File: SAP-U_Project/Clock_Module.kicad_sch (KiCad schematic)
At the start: 22 parts, among them SW1 SW_Wuerth_450301014042, U1 74LS08, U2 LM555xN, U3 LM555xN, U4 LM555xN, U5 74LS32, U6 74LS04

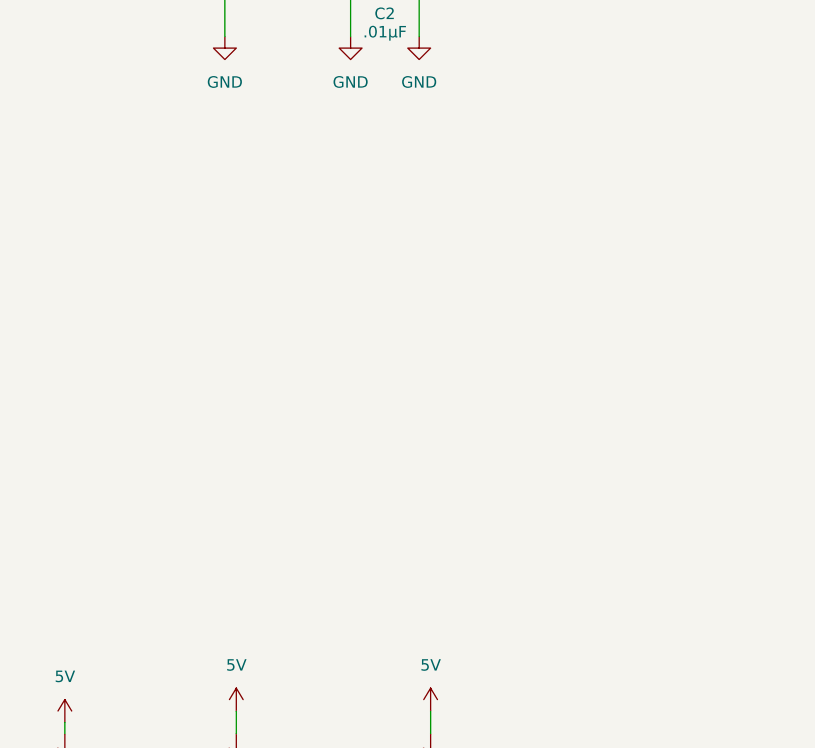
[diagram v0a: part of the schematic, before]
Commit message: Checkpoint: removed simulation, cleaned up schematic
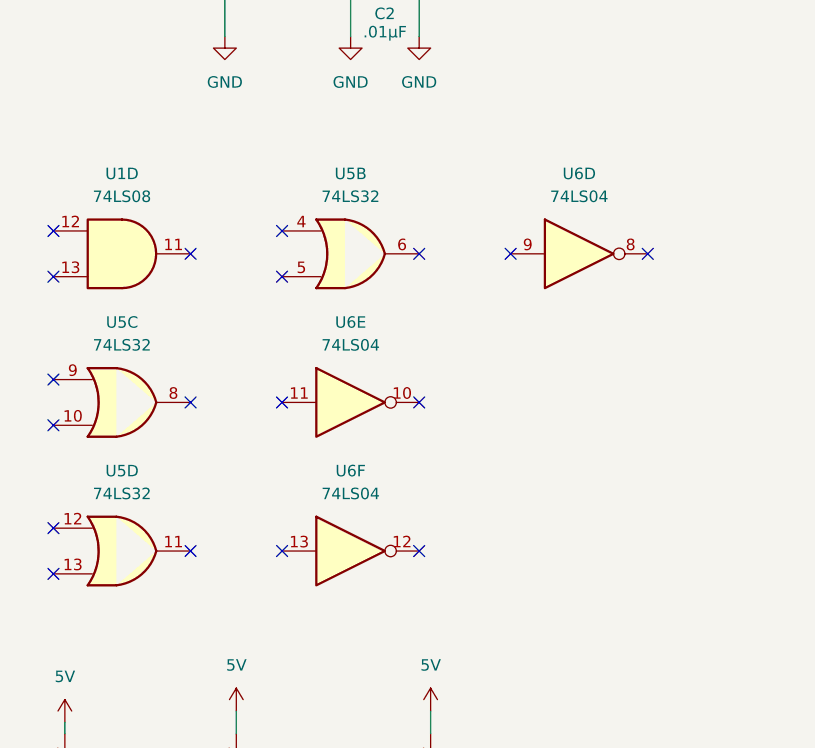
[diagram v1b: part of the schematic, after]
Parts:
- added unit 4 of U1
- added unit 3 of U5
- added unit 4 of U5
- added unit 2 of U5
- added unit 6 of U6
- added unit 5 of U6
- added unit 4 of U6
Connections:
- no-connect marks 2 -> 20
